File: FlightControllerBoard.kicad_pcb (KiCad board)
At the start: 2 copper layers, 60 x 40 mm, 82 parts, among them J1 Conn_01x02, J10 Conn_01x02, J11 Conn_01x02, J12 Conn_01x03_Male, J13 USB_C_Receptacle_USB2.0, J14 Conn_02x03_Odd_Even, J2 Conn_01x03_Male, J3 Conn_01x03_Male, J4 Conn_01x03_Male, J5 Conn_01x03_Male, J6 Conn_01x03_Male, J7 Conn_01x03_Male, J8 Conn_01x03_Male, J9 Conn_01x03_Male, Q1 BSS138, SW1 SW_Push, SW2 SW_Push, U1 FT230XQ, U2 ATmega2560-16AU, U3 BNO055, Y1 16MHz, Y2 32.768kHz

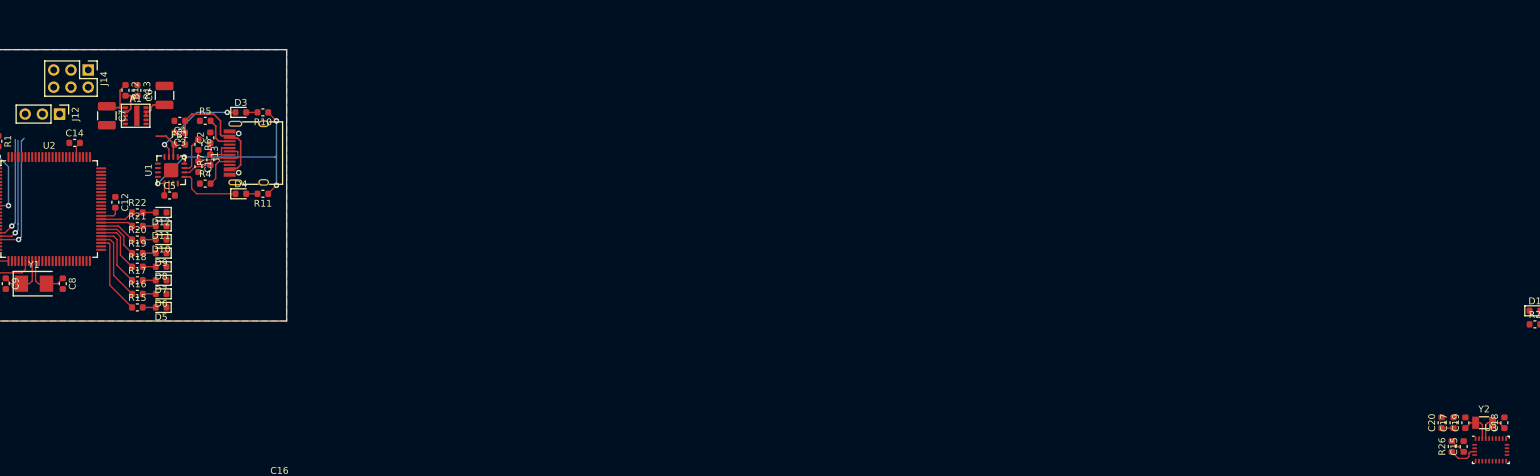
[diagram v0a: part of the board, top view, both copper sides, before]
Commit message: LMZM23600 from official kicad lib
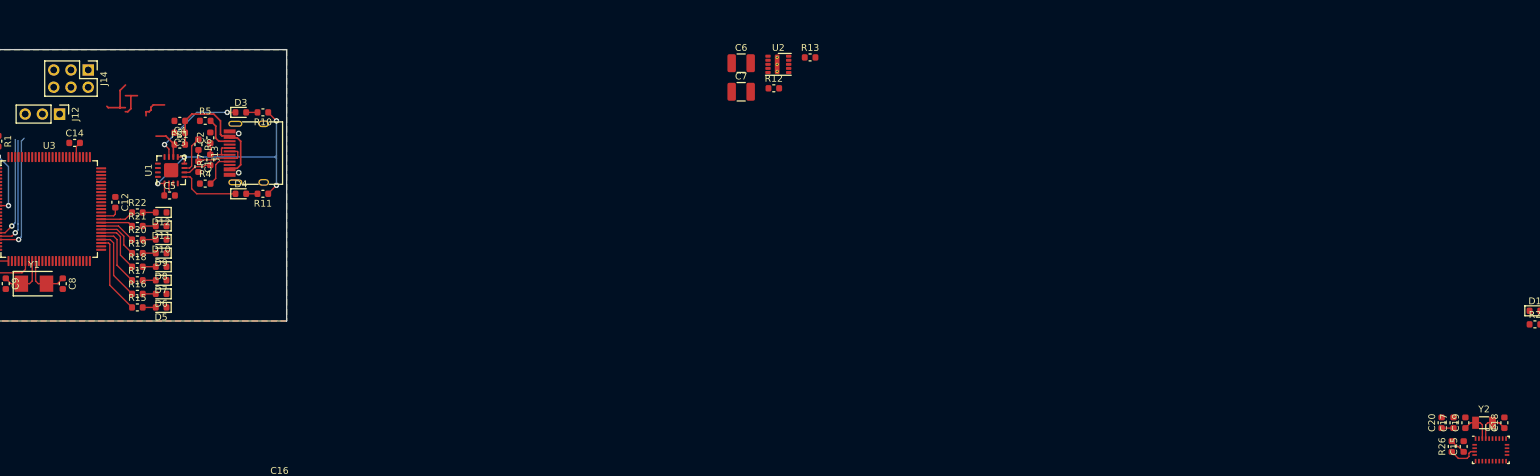
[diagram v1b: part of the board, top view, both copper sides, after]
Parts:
- removed A1: lmzm23600, LMZM23600:lmzm23600
- added U2: LMZM23600, Package_LGA:Texas_SIL0010A_MicroSiP-10-1EP_3.8x3mm_P0.6mm_EP0.7x2.9mm_ThermalVias, F.Cu at (132.5, 2.17)
- moved R13 99.3 mm to (137.2, 1.15), turned to 0 degrees
- moved R12 95.6 mm to (131.8, 5.70), turned to 0 degrees
- moved C7 93.6 mm to (127.0, 6.21), turned to 0 degrees
- moved C6 85.1 mm to (127.0, 2.00), turned to 0 degrees
- renumbered U2 to U3, U3 to U4
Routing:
- net Net-(R12-Pad2): track 4.67 -> 0.00 mm
- net Net-(A1-Pad7): track 0.00 -> 4.67 mm
